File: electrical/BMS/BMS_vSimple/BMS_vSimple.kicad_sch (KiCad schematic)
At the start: 127 parts, among them J1 Conn_01x04_Pin, J2 Conn_02x12_Top_Bottom, J3 Conn_01x13_Socket, Q6 BCP56, U1 STM32F412RGTx, U2 BQ79652PAPRQ1, U3 ISO1044BD, U4 CD74HC4067M

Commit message: updated pcb
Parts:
- added C39, C40, C41, C42, C43: 100n, Capacitor_SMD:C_0603_1608Metric, symbol Device:C
- added H1, H2, H3, H4, H5, H6: MountingHole, MountingHole:MountingHole_2.2mm_M2, symbol Mechanical:MountingHole
- added TP23, TP24: TestPoint, TestPoint:TestPoint_Pad_2.0x2.0mm, symbol Connector:TestPoint
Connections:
- net GND: now also C39.2, C40.2, C41.2, C42.2, C43.2
- net VDD1: now also U1.1 (VBAT), U1.13 (VDDA), U1.32 (VDD), U1.48 (VDD), U1.64 (VDD), C39.1, C40.1, C41.1, C42.1, C43.1
- net at J1.1 (Pin_1): now also U3.5 (CANL); no longer U3.7 (GND2)
- net at J1.2 (Pin_2): now also U3.6 (CANH); no longer U3.5 (CANL)
- net at J1.3 (Pin_3): now also U3.7 (GND2); no longer U3.6 (CANH)
- net at TP7.1: now also U1.49 (PA14); no longer U1.14 (PA0)
- net at U1.33 (PB12): now also TP23.1
- net at U1.37 (PC6): now also TP24.1
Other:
- moved on the sheet: C36, C37, J1, R43, TP1, TP6, TP7, VR1

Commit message: bms is smaller now...
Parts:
- removed J2: Conn_02x12_Top_Bottom, Connector_JST:JST_PHD_B24B-PHDSS_2x12_P2.00mm_Vertical, symbol Connector_Generic:Conn_02x12_Top_Bottom
- added C44: 100n, Capacitor_SMD:C_0603_1608Metric, symbol Device:C
- added C45: 4.7u, Capacitor_SMD:C_0603_1608Metric, symbol Device:C
- added J2: Conn_01x12, Connector_JST:JST_XH_B12B-XH-A_1x12_P2.50mm_Vertical, symbol Connector_Generic:Conn_01x12
- added R54: 10k, Resistor_SMD:R_0603_1608Metric, symbol Device:R
- added TP25, TP26: TestPoint, TestPoint:TestPoint_Pad_2.0x2.0mm, symbol Connector:TestPoint
- J1: footprint Connector_JST:JST_ZH_B4B-ZR_1x04_P1.50mm_Vertical -> Connector_JST:JST_XH_B4B-XH-A_1x04_P2.50mm_Vertical
- J3: footprint Connector_JST:JST_EH_B13B-EH-A_1x13_P2.50mm_Vertical -> Connector_JST:JST_XH_B13B-XH-A_1x13_P2.50mm_Vertical
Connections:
- net GND: now also C44.2, C45.2
- net VDD1: now also R54.1
- net at R45.2, U4.2 (I7): now also J2.8 (Pin_8)
- net at R47.2, U4.9 (I0): now also J2.1 (Pin_1)
- net at R52.2, U4.4 (I5): now also J2.6 (Pin_6)
- net at TP24.1: now also U1.51 (PC10); no longer U1.37 (PC6)
- net at R42.2, U4.22 (I9): now also J2.10 (Pin_10)
- net at R51.2, U4.5 (I4): now also J2.5 (Pin_5)
- net at R41.2, U4.21 (I10): now also J2.11 (Pin_11)
- net at R48.2, U4.8 (I1): now also J2.2 (Pin_2)
- net at R44.2, U4.3 (I6): now also J2.7 (Pin_7)
- net at R46.2, U4.23 (I8): now also J2.9 (Pin_9)
- net at R34.2, U4.20 (I11): now also J2.12 (Pin_12)
- net at R49.2, U4.7 (I2): now also J2.3 (Pin_3)
- net at R50.2, U4.6 (I3): now also J2.4 (Pin_4)
- net at U1.30 (VCAP_1): now also C45.1
- net at U1.46 (PA13): now also TP25.1
- net at U1.60 (BOOT0): now also TP26.1
- net at U1.7 (NRST): now also C44.1, R54.2
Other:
- note added: "Debugging Test points"
- moved on the sheet: TP24

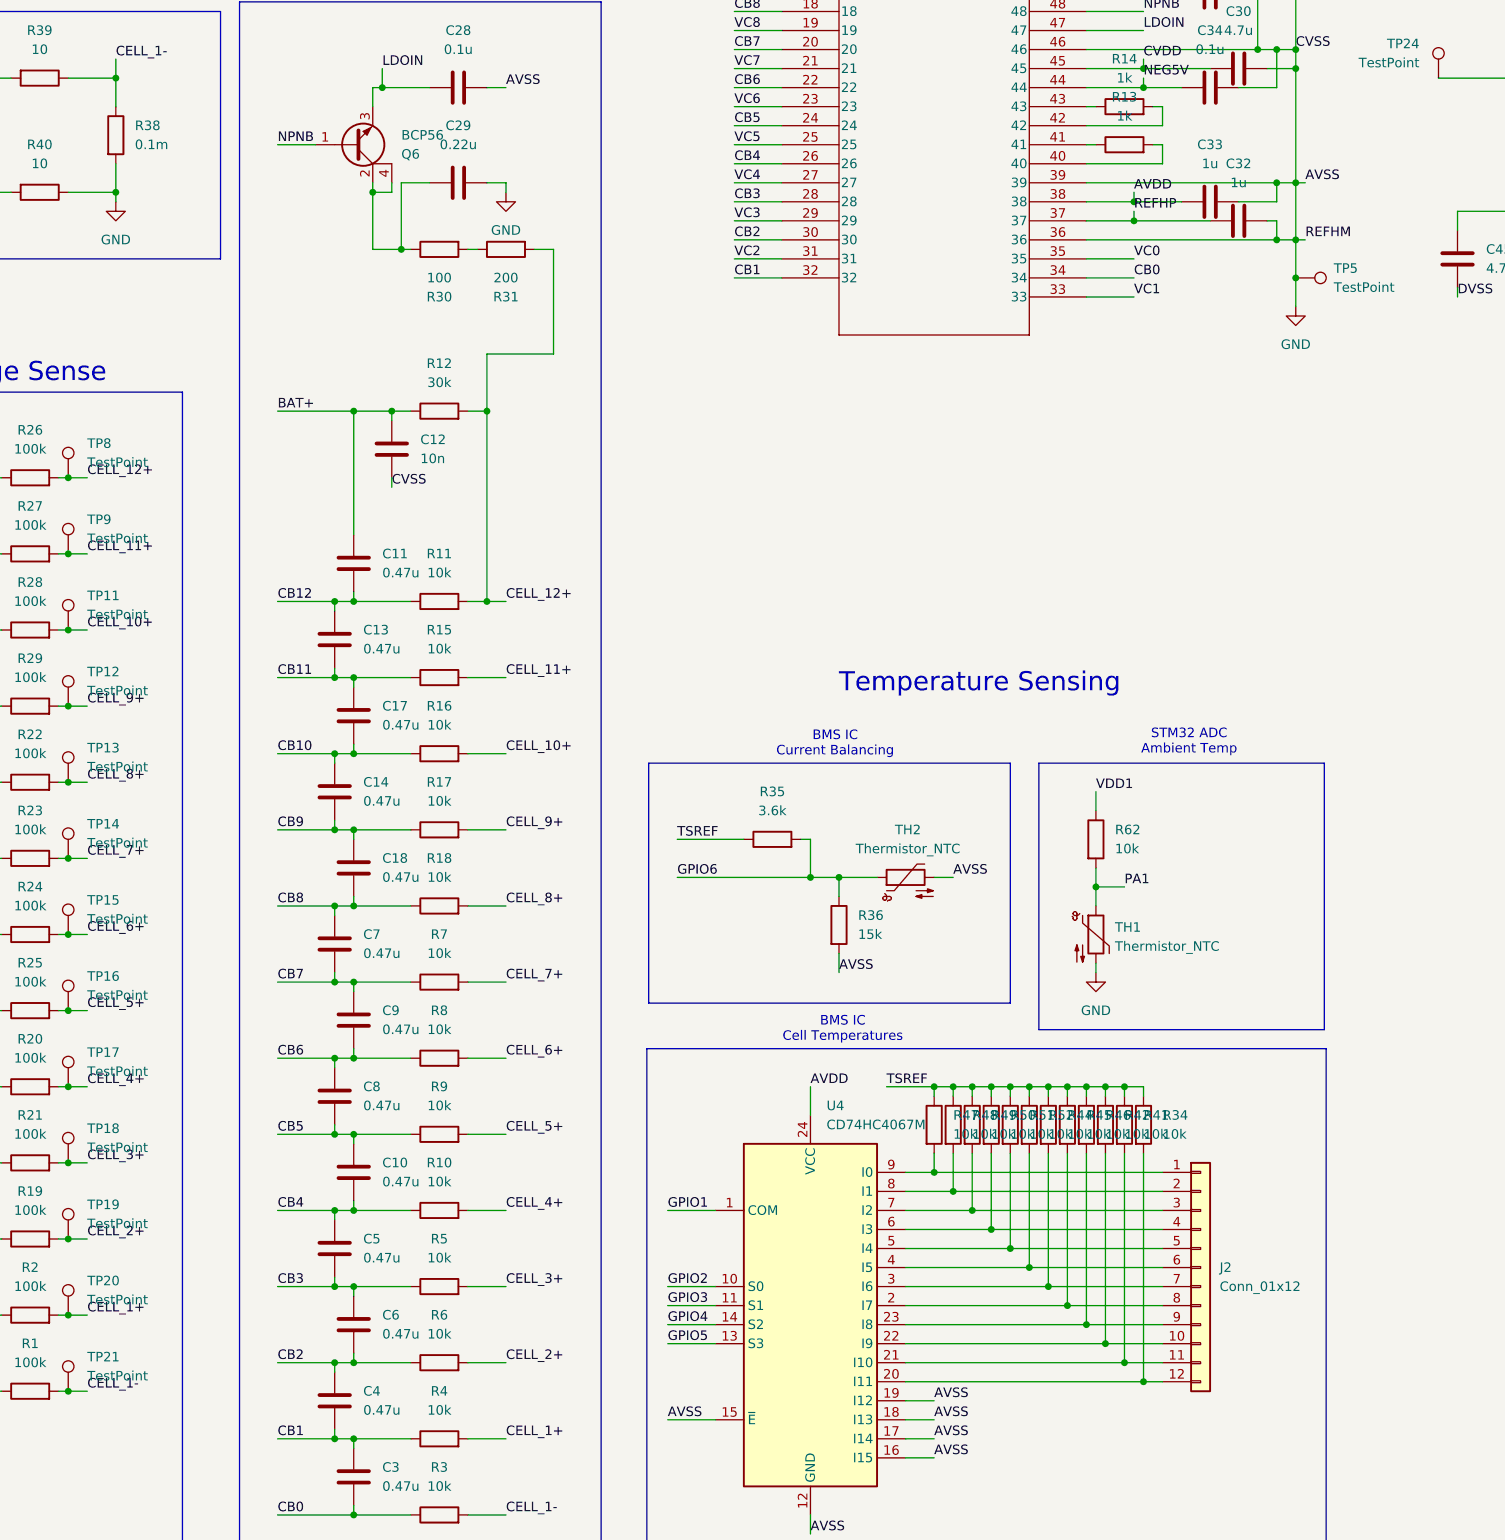
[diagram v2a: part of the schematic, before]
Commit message: bms pcb layout v2
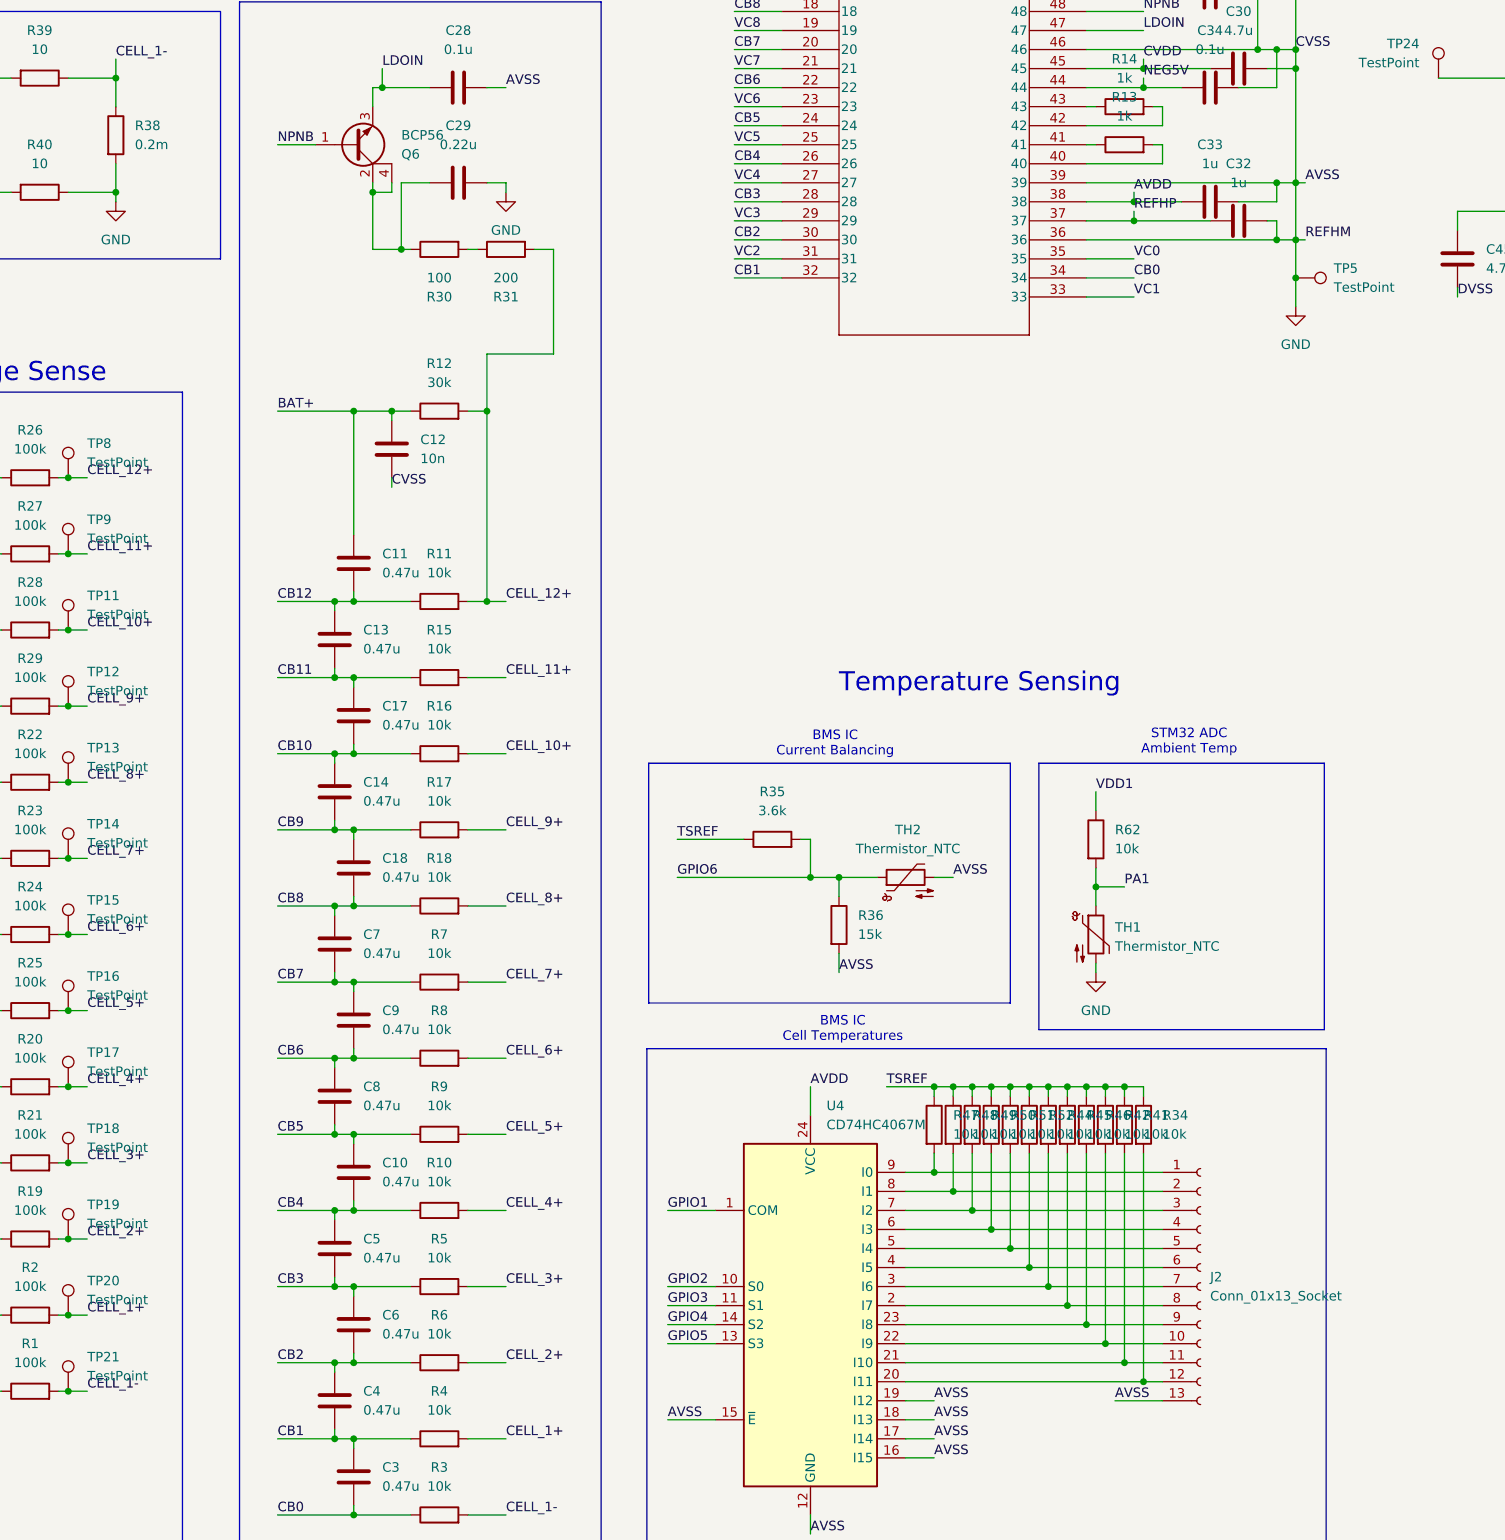
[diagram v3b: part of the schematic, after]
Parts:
- removed J2: Conn_01x12, Connector_JST:JST_XH_B12B-XH-A_1x12_P2.50mm_Vertical, symbol Connector_Generic:Conn_01x12
- added J2: Conn_01x13_Socket, Connector_JST:JST_XH_B13B-XH-A_1x13_P2.50mm_Vertical, symbol Connector:Conn_01x13_Socket
- R38: value 0.1m -> 0.2m; footprint Resistor_SMD:R_0603_1608Metric -> Footprints-Symbols-Models:RESC15077X200N
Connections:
- net GND: now also J2.13 (Pin_13)
- net at R45.2, U4.2 (I7): now also J2.8 (Pin_8)
- net at R47.2, U4.9 (I0): now also J2.1 (Pin_1)
- net at R52.2, U4.4 (I5): now also J2.6 (Pin_6)
- net at R42.2, U4.22 (I9): now also J2.10 (Pin_10)
- net at R51.2, U4.5 (I4): now also J2.5 (Pin_5)
- net at R41.2, U4.21 (I10): now also J2.11 (Pin_11)
- net at R34.2, U4.20 (I11): now also J2.12 (Pin_12)
- net at R48.2, U4.8 (I1): now also J2.2 (Pin_2)
- net at R49.2, U4.7 (I2): now also J2.3 (Pin_3)
- net at R50.2, U4.6 (I3): now also J2.4 (Pin_4)
- net at R44.2, U4.3 (I6): now also J2.7 (Pin_7)
- net at R46.2, U4.23 (I8): now also J2.9 (Pin_9)
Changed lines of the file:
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@@
 	(wire
 		(pts
+			(xy 191.77 256.54) (xy 198.12 256.54)
+		)
+		(stroke
+			(width 0)
+			(type default)
+		)
+	)
+	(wire
+		(pts
 			(xy 143.51 40.64) (xy 147.32 40.64)
 		)
@@
 		)
 	)
+	(label "AVSS"
+		(at 191.77 256.54 0)
+		(effects
+			(font
+				(size 1.27 1.27)
+			)
+			(justify left bottom)
+		)
+	)
 	(label "GPIO1"
 		(at 132.08 231.14 0)
@@
 	)
 	(symbol
+		(lib_id "Connector:Conn_01x13_Socket")
+		(at 203.2 241.3 0)
+		(unit 1)
+		(exclude_from_sim no)
+		(in_bom yes)
+		(on_board yes)
+		(dnp no)
+		(fields_autoplaced yes)
+		(property "Reference" "J2"
+			(at 204.47 240.0299 0)
+			(effects
+				(font
+					(size 1.27 1.27)
+				)
+				(justify left)
+			)
+		)
+		(property "Value" "Conn_01x13_Socket"
+			(at 204.47 242.5699 0)
+			(effects
+				(font
+					(size 1.27 1.27)
+				)
+				(justify left)
+			)
+		)
+		(property "Footprint" "Connector_JST:JST_XH_B13B-XH-A_1x13_P2.50mm_Vertical"
+			(at 203.2 241.3 0)
+			(effects
+				(font
+					(size 1.27 1.27)
+				)
+				(hide yes)
+			)
+		)
+		(property "Datasheet" "~"
+			(at 203.2 241.3 0)
+			(effects
+				(font
+					(size 1.27 1.27)
+				)
+				(hide yes)
+			)
+		)
+		(property "Description" "Generic connector, single row, 01x13, script generated"
+			(at 203.2 241.3 0)
+			(effects
+				(font
+					(size 1.27 1.27)
+				)
+				(hide yes)
+			)
+		)
+		(pin "1"
+		)
+		(pin "2"
+		)
+		(pin "4"
+		)
+		(pin "9"
+		)
+		(pin "11"
+		)
+		(pin "6"
+		)
+		(pin "10"
+		)
+		(pin "3"
+		)
+		(pin "8"
+		)
+		(pin "5"
+		)
+		(pin "7"
+		)
+		(pin "13"
+		)
+		(pin "12"
+		)
+		(instances
+			(project "BMS_vSimple"
+				(path "/4b24ec67-0839-44fd-9d23-6940e755155f"
+					(reference "J2")
+					(unit 1)
+				)
+			)
+		)
+	)
+	(symbol
 		(lib_id "Device:R")
 		(at 177.8 219.71 0)
@@
 	)
 	(symbol
-		(lib_id "Connector_Generic:Conn_01x12")
-		(at 203.2 238.76 0)
-		(unit 1)
-		(exclude_from_sim no)
-		(in_bom yes)
-		(on_board yes)
-		(dnp no)
-		(fields_autoplaced yes)
-		(property "Reference" "J2"
-			(at 205.74 238.7599 0)
-			(effects
-				(font
-					(size 1.27 1.27)
-				)
-				(justify left)
-			)
-		)
-		(property "Value" "Conn_01x12"
-			(at 205.74 241.2999 0)
-			(effects
-				(font
-					(size 1.27 1.27)
-				)
-				(justify left)
-			)
-		)
-		(property "Footprint" "Connector_JST:JST_XH_B12B-XH-A_1x12_P2.50mm_Vertical"
-			(at 203.2 238.76 0)
-			(effects
-				(font
-					(size 1.27 1.27)
-				)
-				(hide yes)
-			)
-		)
-		(property "Datasheet" "~"
-			(at 203.2 238.76 0)
-			(effects
-				(font
-					(size 1.27 1.27)
-				)
-				(hide yes)
-			)
-		)
-		(property "Description" "Generic connector, single row, 01x12, script generated (kicad-library-utils/schlib/autogen/connector/)"
-			(at 203.2 238.76 0)
-			(effects
-				(font
-					(size 1.27 1.27)
-				)
-				(hide yes)
-			)
-		)
-		(pin "3"
-		)
-		(pin "5"
-		)
-		(pin "12"
-		)
-		(pin "6"
-		)
-		(pin "9"
-		)
-		(pin "8"
-		)
-		(pin "7"
-		)
-		(pin "11"
-		)
-		(pin "1"
-		)
-		(pin "2"
-		)
-		(pin "4"
-		)
-		(pin "10"
-		)
-		(instances
-			(project ""
-				(path "/4b24ec67-0839-44fd-9d23-6940e755155f"
-					(reference "J2")
-					(unit 1)
-				)
-			)
-		)
-	)
-	(symbol
 		(lib_id "Device:C")
 		(at 104.14 93.98 90)
@@
 			)
 		)
-		(property "Value" "0.1m"
+		(property "Value" "0.2m"
 			(at 60.96 88.8999 0)
 			(effects
@@
 			)
 		)
-		(property "Footprint" "Resistor_SMD:R_0603_1608Metric"
+		(property "Footprint" "Footprints-Symbols-Models:RESC15077X200N"
 			(at 56.642 87.63 90)
 			(effects
